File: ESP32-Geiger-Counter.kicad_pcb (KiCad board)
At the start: 2 copper layers, 160 x 117 mm, 85 parts, among them J1 2s1p Lipo Battery Pack (8.4V-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, J2 USB_C_Receptacle_USB2.0_16P, J5 Conn_01x07, Q1 STN1HNK60, Q3 2N7002, Q4 AO3401A, Q5 MMBT3904, SW1 SW_SPDT, SW2 RESET, SW3 BOOT, U1 BQ25886RGE, U2 AP63203WU, U3 ESP32-S3-WROOM-1, U4 UCC27517DBVR, U5 USBLC6-2SC6, U6 SBM-20 Geiger Mueller Tube

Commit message: saving layout stuff
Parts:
- moved C27 341.4 mm to (103.4, 213.3), turned to 180 degrees
- moved C25 328.0 mm to (119.0, 214.0), turned to 90 degrees
- moved C24 322.1 mm to (115.0, 214.0), turned to 90 degrees
- moved D6 319.9 mm to (111.0, 232.5), turned to -90 degrees
- moved D5 318.9 mm to (111.0, 225.0), turned to -90 degrees
- moved D4 317.9 mm to (111.0, 217.5), turned to -90 degrees
- moved Q1 316.0 mm to (136.3, 221.8), turned to 180 degrees
- moved R19 312.8 mm to (105.0, 210.1), turned to 90 degrees
- moved U4 310.0 mm to (138.1, 232.0)
- moved R17 308.1 mm to (106.6, 230.6)
- moved D3 306.2 mm to (124.5, 215.5)
- moved R14 290.3 mm to (105.5, 219.0)
- moved R15 290.1 mm to (105.5, 222.0), turned to 180 degrees
- moved R16 288.9 mm to (107.5, 226.7), turned to 90 degrees
- moved R24 288.5 mm to (135.5, 235.6), turned to 90 degrees
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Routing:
- added copper zone on F.Cu, net +3.3V
- added copper zone on F.Cu, net /VSYS_SW
- added copper zone on F.Cu, net GND
- added copper zone on F.Cu, net Net-(U2-BST)
- added copper zone on F.Cu, net Net-(U2-SW)
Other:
- board size 160 x 117 mm -> 137 x 117 mm

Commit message: board layout changes
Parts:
- SW2, SW3: footprint Button_Switch_SMD:SW_SPST_TL3342 -> Button_Switch_THT:SW_PUSH_6mm
- moved C23 318.5 mm to (128.0, 235.5), turned to -90 degrees
- moved C30 313.9 mm to (146.3, 249.0), turned to 180 degrees
- moved R28 284.7 mm to (188.8, 296.0)
- moved R1 266.3 mm to (205.9, 295.2), turned to 180 degrees
- moved R2 260.6 mm to (211.0, 295.1), turned to 180 degrees
- moved C31 256.2 mm to (146.2, 251.5), turned to 180 degrees
- moved R27 248.0 mm to (186.2, 225.8)
- moved R26 248.0 mm to (186.2, 222.8)
- moved C19 241.8 mm to (225.0, 246.5)
- moved R13 241.5 mm to (208.3, 271.5)
- moved R25 238.5 mm to (186.8, 229.9)
- moved C21 238.4 mm to (225.0, 244.0)
- moved R10 225.1 mm to (210.1, 238.0)
- moved R11 225.1 mm to (210.1, 240.9)
- moved R12 219.5 mm to (220.7, 248.8), turned to 180 degrees
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
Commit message: working on layout
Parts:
- J1: moved to B.Cu
- moved J1 148.2 mm to (219.6, 300.6), turned to 0 degrees
- moved C9 110.5 mm to (197.6, 261.3), turned to 90 degrees
- moved C13 104.2 mm to (195.6, 261.3), turned to -90 degrees
- moved R9 103.6 mm to (191.5, 261.3), turned to -90 degrees
- moved C8 103.6 mm to (199.8, 260.1), turned to -90 degrees
- moved C7 102.5 mm to (198.0, 255.3), turned to -90 degrees
- moved R3 99.4 mm to (186.9, 260.1), turned to -90 degrees
- moved R8 98.3 mm to (188.6, 252.8), turned to 180 degrees
- moved D2 96.4 mm to (191.5, 264.8), turned to -90 degrees
- moved C12 95.3 mm to (191.6, 250.3), turned to -90 degrees
- moved C32 95.3 mm to (200.4, 255.3), turned to -90 degrees
- moved R5 94.6 mm to (193.6, 261.3), turned to -90 degrees
- moved R4 92.1 mm to (188.6, 255.8)
- moved R6 91.7 mm to (189.1, 261.3), turned to 90 degrees
- moved D1 90.9 mm to (185.1, 252.8), turned to 180 degrees
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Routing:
- net Net-(U1-TS): track 0.00 -> 8.31 mm
- net Net-(U1-ILIM): track 0.00 -> 5.56 mm
- net Net-(U1-BTST): track 0.00 -> 5.04 mm
- net Net-(U1-~{PG}): track 0.00 -> 4.98 mm
- net /REGN: track 0.00 -> 4.71 mm
- net Net-(U1-ICHGSET): track 0.00 -> 3.70 mm
- net Net-(U1-STAT): track 0.00 -> 2.37 mm
- net Net-(U1-VSET): track 0.00 -> 1.95 mm
- net Net-(D1-K): track 0.00 -> 1.69 mm
- net Net-(D2-K): track 0.00 -> 1.64 mm
- added copper zone on F.Cu, net +5V
- added copper zone on F.Cu, net /BATT
- added copper zone on F.Cu, net /SYS
- added copper zone on F.Cu, net Net-(C10-Pad2)
- added copper zone on F.Cu, net Net-(C9-Pad1)
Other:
- board size 137 x 117 mm -> 137 x 104 mm

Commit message: huge layout changes
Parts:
- moved SW2 48.6 mm to (215.7, 239.3)
- moved SW3 31.5 mm to (215.4, 247.7)
- moved Q3 31.0 mm to (200.2, 261.7)
- moved R27 31.0 mm to (201.1, 264.8)
- moved R26 31.0 mm to (197.2, 264.8)
- moved C13 27.5 mm to (197.6, 288.7)
- moved C9 27.5 mm to (199.6, 288.7)
- moved R5 27.5 mm to (195.6, 288.7)
- moved R6 27.5 mm to (191.1, 288.7)
- moved R9 27.5 mm to (193.5, 288.7)
- moved R3 27.5 mm to (188.9, 287.5)
- moved R7 27.5 mm to (186.8, 287.5)
- moved C10 27.5 mm to (197.1, 275.8)
- moved C11 27.5 mm to (197.1, 278.3)
- moved L1 27.5 mm to (197.6, 272.3)
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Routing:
- net /D-: track 0.00 -> 70.0 mm, vias 0 -> 6
- net /D+: track 0.00 -> 68.8 mm, vias 0 -> 6
- net +5V: track 0.00 -> 36.2 mm, vias 0 -> 2
- net /SYS: track 0.00 -> 32.3 mm, vias 0 -> 2
- net /VSYS_SW: track 0.00 -> 25.8 mm
- net /REGN: track 4.71 -> 30.3 mm
- net /BATT: track 0.00 -> 18.7 mm
- net Net-(F1-Pad2): track 0.00 -> 13.3 mm, vias 0 -> 2
- net Net-(Q4-G): track 0.00 -> 12.3 mm, vias 0 -> 2
- net Net-(C9-Pad1): track 0.00 -> 11.9 mm, vias 0 -> 2
- net Net-(J2-D+-PadA6): track 0.00 -> 11.6 mm
- net Net-(J2-D--PadA7): track 0.00 -> 10.2 mm
- net GND: track 0.00 -> 9.33 mm, vias 0 -> 1
- net Net-(J2-CC1): track 0.00 -> 6.91 mm
- net Net-(J2-CC2): track 0.00 -> 6.67 mm
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- added copper zone on B.Cu, net GND

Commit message: layout stuff
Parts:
- moved C23 62.2 mm to (66.9, 246.6)
- moved C28 62.2 mm to (71.2, 246.6)
- moved C29 62.2 mm to (69.2, 246.6)
- moved U4 62.2 mm to (74.3, 247.2)
- moved R24 61.3 mm to (72.3, 242.8)
- moved R23 59.8 mm to (78.3, 244.9)
- moved D4 51.0 mm to (62.0, 211.7)
- moved D5 51.0 mm to (62.0, 219.2)
- moved D6 51.0 mm to (62.0, 226.7)
- moved R14 51.0 mm to (56.5, 213.2)
- moved R15 51.0 mm to (56.5, 216.2)
- moved R16 51.0 mm to (58.5, 220.9)
- moved R18 51.0 mm to (58.3, 208.8)
- moved C24 51.0 mm to (66.0, 208.2)
- moved C25 51.0 mm to (70.0, 208.2)
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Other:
- board size 137 x 104 mm -> 137 x 88 mm

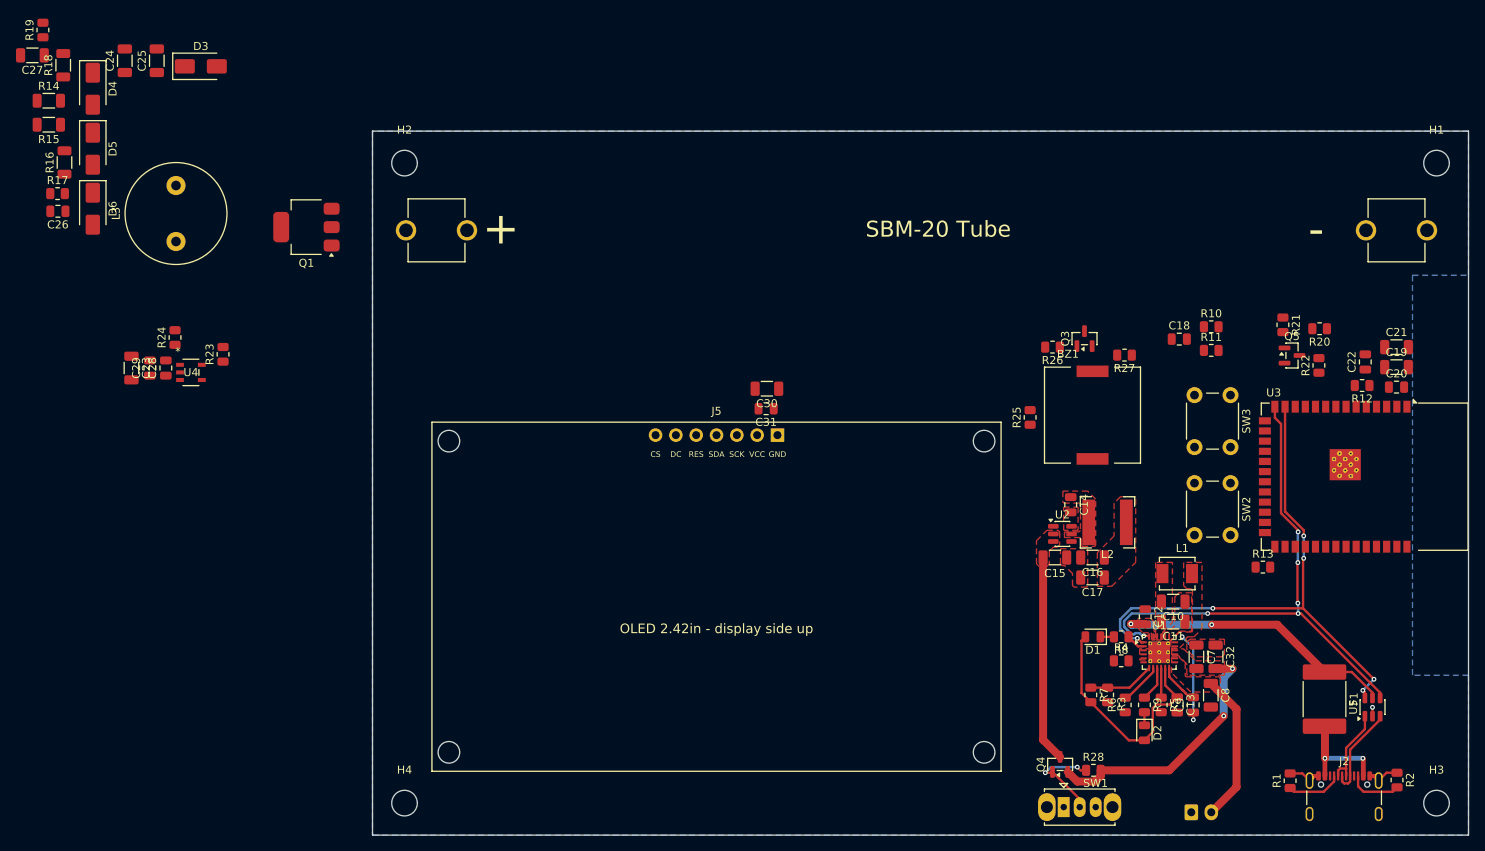
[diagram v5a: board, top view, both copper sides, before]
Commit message: added 400v boost to board
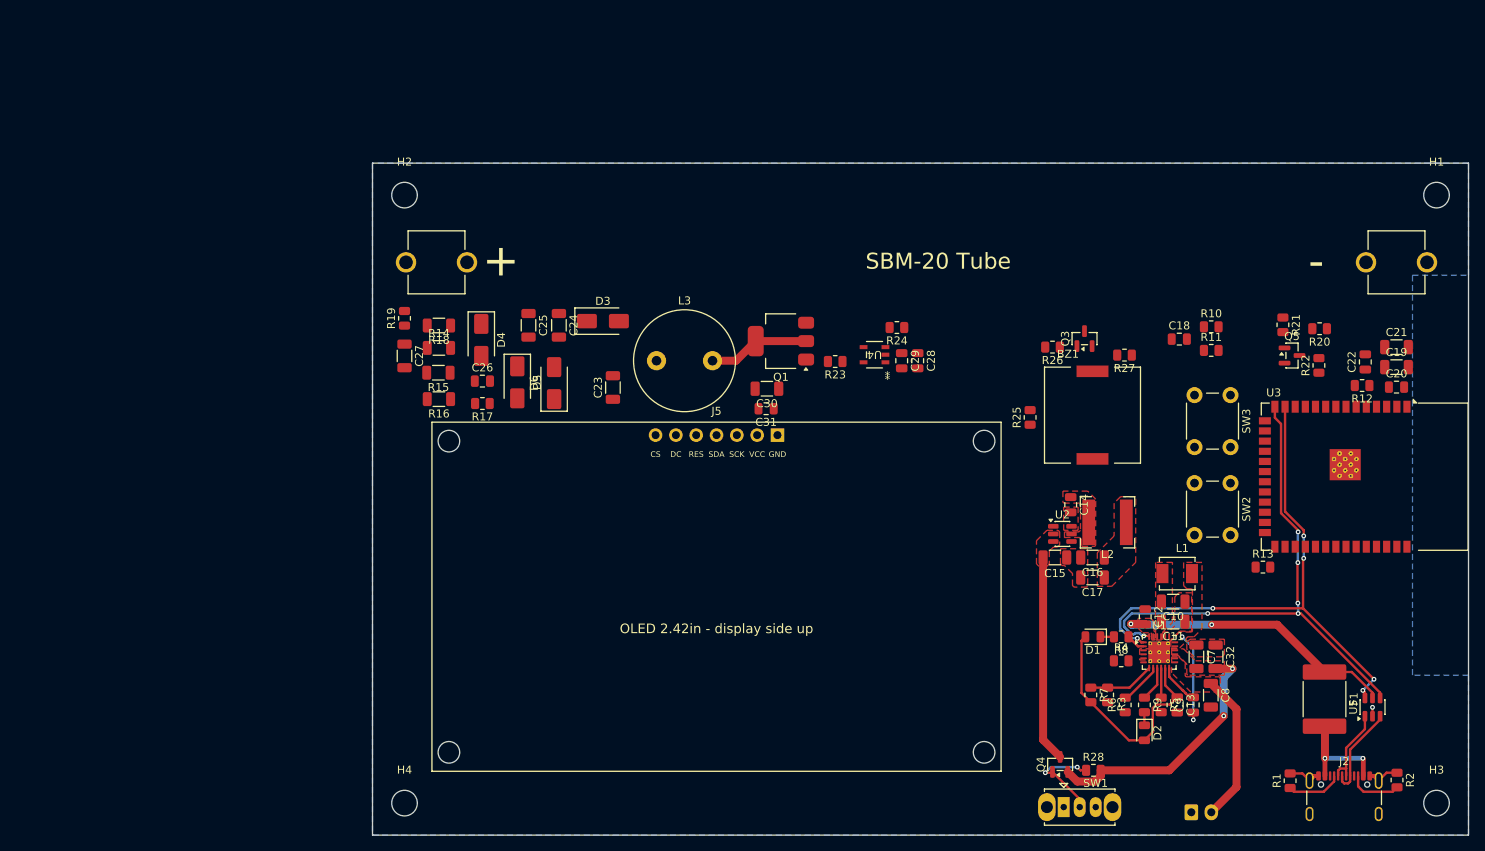
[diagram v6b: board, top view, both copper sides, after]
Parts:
- moved C28 94.0 mm to (165.2, 245.7), turned to -90 degrees
- moved C29 94.0 mm to (163.2, 245.7), turned to -90 degrees
- moved R24 90.2 mm to (162.6, 241.6), turned to 180 degrees
- moved U4 85.5 mm to (159.8, 244.9), turned to 180 degrees
- moved R23 76.5 mm to (154.8, 245.8), turned to 180 degrees
- moved C24 63.5 mm to (120.3, 241.3), turned to -90 degrees
- moved L3 61.9 mm to (132.5, 245.7), turned to 0 degrees
- moved D6 61.6 mm to (119.7, 248.5), turned to 90 degrees
- moved Q1 61.0 mm to (148.1, 243.2)
- moved D5 60.6 mm to (115.1, 248.4)
- moved C23 60.2 mm to (127.0, 249.1), turned to 90 degrees
- moved C27 59.8 mm to (101.0, 245.1), turned to -90 degrees
- moved D3 59.5 mm to (125.8, 240.8)
- moved R17 59.2 mm to (110.7, 251.1), turned to 180 degrees
- moved D4 57.8 mm to (110.6, 243.1)
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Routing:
- net Net-(D3-A): track 0.00 -> 12.7 mm
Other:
- board size 137 x 88 mm -> 137 x 84 mm

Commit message: layout save
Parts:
- moved L3 5.62 mm to (136.6, 249.6), turned to 90 degrees
- moved R27 1.41 mm to (190.1, 244.0), turned to 90 degrees
- moved C23 1.11 mm to (127.7, 249.9)
- moved Q3 1.11 mm to (186.8, 243.8)
- moved R26 1.11 mm to (182.8, 244.8)
- moved R25 1.07 mm to (178.4, 253.5)
- moved BZ1 0.85 mm to (186.2, 252.8)
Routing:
- net /VSYS_SW: track 25.8 -> 112.4 mm
- net Net-(BZ1--): track 0.00 -> 9.40 mm
- net Net-(U3-IO0): track 0.00 -> 2.80 mm
- net Net-(Q3-G): track 0.00 -> 2.19 mm
- net Net-(D3-A): track 12.7 -> 14.9 mm
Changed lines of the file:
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@@
 	(footprint "Resistor_SMD:R_0805_2012Metric"
 		(layer "F.Cu")
-		(at 182 244 180)
+		(at 182.75 244.8125 180)
 		(descr "Resistor SMD 0805 (2012 Metric), square (rectangular) end terminal, IPC-7351 nominal, (Body size source: IPC-SM-782 page 72, https://www.pcb-3d.com/wordpress/wp-content/uploads/ipc-sm-782a_amendment_1_and_2.pdf)")
 		(tags "resistor")
@@
 	(footprint "Inductor_THT:L_Radial_D12.5mm_P7.00mm_Fastron_09HCP"
 		(layer "F.Cu")
-		(at 132.5 245.7)
+		(at 136.6 249.55 90)
 		(descr "Inductor, Radial series, Radial, pin pitch=7.00mm, diameter=12.5mm, height=10.8mm, Fastron, 09HCP, http://cdn-reichelt.de/documents/datenblatt/B400/DS_09HCP.pdf")
 		(tags "Inductor Radial series Radial pin pitch 7.00mm  diameter 12.5mm height 10.8mm Fastron 09HCP")
 		(property "Reference" "L3"
-			(at 3.5 -7.5 0)
+			(at 3.5 -7.5 90)
 			(layer "F.SilkS")
 			(effects
@@
 		)
 		(property "Value" "10mH"
-			(at 3.5 7.5 0)
+			(at 3.5 7.5 90)
 			(layer "F.Fab")
 			(effects
@@
 		)
 		(property "Datasheet" ""
-			(at 0 0 0)
+			(at 0 0 90)
 			(layer "F.Fab")
 			(hide yes)
@@
 		)
 		(property "Description" "Inductor"
-			(at 0 0 0)
+			(at 0 0 90)
 			(layer "F.Fab")
 			(hide yes)
@@
 		)
 		(property "KiLib_Generator" "choke_THT"
-			(at 0 0 0)
+			(at 0 0 90)
 			(layer "F.SilkS")
 			(hide yes)
@@
 		)
 		(fp_text user "${REFERENCE}"
-			(at 3.5 0 0)
+			(at 3.5 0 90)
 			(layer "F.Fab")
 			(effects
@@
 		)
 		(pad "1" thru_hole circle
-			(at 0 0)
+			(at 0 0 90)
 			(size 2.4 2.4)
 			(drill 1.2)
@@
 		)
 		(pad "2" thru_hole circle
-			(at 7 0)
+			(at 7 0 90)
 			(size 2.4 2.4)
 			(drill 1.2)
@@
 	(footprint "Resistor_SMD:R_0805_2012Metric"
 		(layer "F.Cu")
-		(at 191 245 180)
+		(at 190.05 243.9625 90)
 		(descr "Resistor SMD 0805 (2012 Metric), square (rectangular) end terminal, IPC-7351 nominal, (Body size source: IPC-SM-782 page 72, https://www.pcb-3d.com/wordpress/wp-content/uploads/ipc-sm-782a_amendment_1_and_2.pdf)")
 		(tags "resistor")
 		(property "Reference" "R27"
-			(at 0 -1.65 0)
+			(at 0 -1.65 90)
 			(layer "F.SilkS")
 			(effects
@@
 		)
 		(property "Value" "100k"
-			(at 0 1.65 0)
+			(at 0 1.65 90)
 			(layer "F.Fab")
 			(effects
@@
 		)
 		(property "Datasheet" ""
-			(at 0 0 0)
+			(at 0 0 90)
 			(layer "F.Fab")
 			(hide yes)
@@
 		)
 		(property "Description" "Resistor, US symbol"
-			(at 0 0 0)
+			(at 0 0 90)
 			(layer "F.Fab")
 			(hide yes)
@@
 		)
 		(property "KiLib_Generator" "SMD_2terminal_chip_molded"
-			(at 0 0 0)
+			(at 0 0 90)
 			(layer "F.SilkS")
 			(hide yes)
@@
 		(duplicate_pad_numbers_are_jumpers no)
 		(fp_line
-			(start -0.227064 0.735)
-			(end 0.227064 0.735)
+			(start -0.227064 -0.735)
+			(end 0.227064 -0.735)
 			(stroke
 				(width 0.12)
@@
 		)
 		(fp_line
-			(start -0.227064 -0.735)
-			(end 0.227064 -0.735)
+			(start -0.227064 0.735)
+			(end 0.227064 0.735)
 			(stroke
 				(width 0.12)
@@
 		)
 		(fp_text user "${REFERENCE}"
-			(at 0 0 0)
+			(at 0 0 90)
 			(layer "F.Fab")
 			(effects
@@
 		)
 		(pad "1" smd roundrect
-			(at -0.9125 0 180)
+			(at -0.9125 0 90)
 			(size 1.025 1.4)
 			(layers "F.Cu" "F.Mask" "F.Paste")
@@
 		)
 		(pad "2" smd roundrect
-			(at 0.9125 0 180)
+			(at 0.9125 0 90)
 			(size 1.025 1.4)
 			(layers "F.Cu" "F.Mask" "F.Paste")
@@
 	(footprint "Resistor_SMD:R_0805_2012Metric"
 		(layer "F.Cu")
-		(at 179.2 252.7875 90)
+		(at 178.4 253.5 90)
 		(descr "Resistor SMD 0805 (2012 Metric), square (rectangular) end terminal, IPC-7351 nominal, (Body size source: IPC-SM-782 page 72, https://www.pcb-3d.com/wordpress/wp-content/uploads/ipc-sm-782a_amendment_1_and_2.pdf)")
 		(tags "resistor")
@@
 	(footprint "Package_TO_SOT_SMD:SOT-23"
 		(layer "F.Cu")
-		(at 186 242.9375 90)
+		(at 186.75 243.75 90)
 		(descr "SOT, 3 Pin (JEDEC TO-236 Var AB https://www.jedec.org/document_search?search_api_views_fulltext=TO-236)")
 		(tags "SOT TO_SOT_SMD")
@@
 	(footprint "CPT_1203_78_SMT_TR:XDCR_CPT-1203-78-SMT-TR"
 		(layer "F.Cu")
-		(at 187 252.5)
+		(at 186.2 252.8)
 		(property "Reference" "BZ1"
 			(at -3.075 -7.635 0)
@@
 	(footprint "Capacitor_SMD:C_1206_3216Metric"
 		(layer "F.Cu")
-		(at 127.05 249.05 90)
+		(at 127.7 249.95 90)
 		(descr "Capacitor SMD 1206 (3216 Metric), square (rectangular) end terminal, IPC-7351 nominal, (Body size source: IPC-SM-782 page 76, https://www.pcb-3d.com/wordpress/wp-content/uploads/ipc-sm-782a_amendment_1_and_2.pdf)")
 		(tags "capacitor")
@@
 	)
 	(segment
+		(start 183.6625 244.8125)
+		(end 185.675 244.8125)
+		(width 0.3)
+		(layer "F.Cu")
+		(net "Net-(Q3-G)")
+	)
+	(segment
+		(start 185.675 244.8125)
+		(end 185.8 244.6875)
+		(width 0.3)
+		(layer "F.Cu")
+		(net "Net-(Q3-G)")
+	)
+	(segment
 		(start 187.9875 280.2125)
 		(end 189.675 280.2125)
@@
 	)
 	(segment
+		(start 165.15 246.65)
+		(end 169.9 246.65)
+		(width 1)
+		(layer "F.Cu")
+		(net "/VSYS_SW")
+	)
+	(segment
+		(start 169.9 246.65)
+		(end 177 253.75)
+		(width 1)
+		(layer "F.Cu")
+		(net "/VSYS_SW")
+	)
+	(segment
+		(start 134.725 251.425)
+		(end 136.6 249.55)
+		(width 1)
+		(layer "F.Cu")
+		(net "/VSYS_SW")
+	)
+	(segment
+		(start 177 253.75)
+		(end 177 266.475)
+		(width 1)
+		(layer "F.Cu")
+		(net "/VSYS_SW")
+	)
+	(segment
+		(start 178.1625 252.5875)
+		(end 177 253.75)
+		(width 1)
+		(layer "F.Cu")
+		(net "/VSYS_SW")
+	)
+	(segment
+		(start 186.2 247.325)
+		(end 183.6625 247.325)
+		(width 0.3)
+		(layer "F.Cu")
+		(net "/VSYS_SW")
+	)
+	(segment
 		(start 180.825 293.1)
 		(end 182.95 295.225)
@@
 	)
 	(segment
+		(start 127.7 251.425)
+		(end 134.725 251.425)
+		(width 1)
+		(layer "F.Cu")
+		(net "/VSYS_SW")
+	)
+	(segment
+		(start 177 266.475)
+		(end 180.825 270.3)
+		(width 1)
+		(layer "F.Cu")
+		(net "/VSYS_SW")
+	)
+	(segment
+		(start 162.400001 245.900001)
+		(end 163.15 246.65)
+		(width 0.5)
+		(layer "F.Cu")
+		(net "/VSYS_SW")
+	)
+	(segment
+		(start 178.4 252.5875)
+		(end 178.1625 252.5875)
+		(width 1)
+		(layer "F.Cu")
+		(net "/VSYS_SW")
+	)
+	(segment
+		(start 136.6 249.55)
+		(end 138.55 247.6)
+		(width 1)
+		(layer "F.Cu")
+		(net "/VSYS_SW")
+	)
+	(segment
+		(start 138.55 247.6)
+		(end 162.2 247.6)
+		(width 1)
+		(layer "F.Cu")
+		(net "/VSYS_SW")
+	)
+	(segment
+		(start 161.11525 245.900001)
+		(end 162.400001 245.900001)
+		(width 0.5)
+		(layer "F.Cu")
+		(net "/VSYS_SW")
+	)
+	(segment
 		(start 180.825 270.3)
 		(end 180.825 293.1)
@@
 	)
 	(segment
+		(start 162.2 247.6)
+		(end 163.15 246.65)
+		(width 1)
+		(layer "F.Cu")
+		(net "/VSYS_SW")
+	)
+	(segment
+		(start 183.6625 247.325)
+		(end 178.4 252.5875)
+		(width 0.3)
+		(layer "F.Cu")
+		(net "/VSYS_SW")
+	)
+	(segment
+		(start 163.15 246.65)
+		(end 165.15 246.65)
+		(width 1)
+		(layer "F.Cu")
+		(net "/VSYS_SW")
+	)
+	(segment
 		(start 222.195 297.605567)
 		(end 222.77 298.180567)
@@
 	)
 	(segment
-		(start 139.5 245.7)
-		(end 142.45 245.7)
+		(start 144.9 243.25)
+		(end 151.2 243.25)
 		(width 1)
 		(layer "F.Cu")
@@
 	)
 	(segment
-		(start 144.9 243.25)
-		(end 151.2 243.25)
+		(start 144.2 242.55)
+		(end 144.9 243.25)
 		(width 1)
 		(layer "F.Cu")
@@
 	)
 	(segment
-		(start 142.45 245.7)
-		(end 144.9 243.25)
+		(start 136.6 242.55)
+		(end 144.2 242.55)
 		(width 1)
 		(layer "F.Cu")
@@
 	)
 	(segment
+		(start 209.2125 271.5)
+		(end 209.2125 269.531721)
+		(width 0.3)
+		(layer "F.Cu")
+		(net "Net-(U3-IO0)")
+	)
+	(segment
+		(start 209.2125 269.531721)
+		(end 209.797229 268.946992)
+		(width 0.3)
+		(layer "F.Cu")
+		(net "Net-(U3-IO0)")
+	)
+	(segment
 		(start 181.9 297.2)
 		(end 182 297.1)
@@
 	)
 	(segment
+		(start 186.2 258.275)
+		(end 182.2625 258.275)
+		(width 0.3)
+		(layer "F.Cu")
+		(net "Net-(BZ1--)")
+	)
+	(segment
+		(start 182.2625 258.275)
+		(end 178.4 254.4125)
+		(width 0.3)
+		(layer "F.Cu")
+		(net "Net-(BZ1--)")
+	)
+	(segment

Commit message: some wiring
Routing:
- net Net-(D3-K): track 0.00 -> 20.9 mm
- net Net-(U6-A): track 0.00 -> 16.5 mm
- net Net-(D3-A): track 14.9 -> 24.4 mm
- net /HV_SENSE: track 0.00 -> 6.11 mm
- net Net-(C27-Pad1): track 0.00 -> 5.16 mm
- net Net-(D4-A): track 0.00 -> 5.04 mm
- net Net-(D5-A): track 0.00 -> 4.64 mm
- net Net-(R15-Pad1): track 0.00 -> 4.49 mm
- net Net-(R14-Pad1): track 0.00 -> 3.13 mm
- net Net-(Q1-G): track 0.00 -> 2.83 mm
- net Net-(U4-OUT): track 0.00 -> 2.68 mm
- net /HV_PWM: track 0.00 -> 2.67 mm
